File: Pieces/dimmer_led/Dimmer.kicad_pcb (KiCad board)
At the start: 2 copper layers, 83 x 60 mm, 41 parts, among them J1 Conn_01x02_Female, J2 Conn_01X03, J3 TB_1X2, J4 Conn_01x03_Female, J5 TB_1X2, J6 TB_1X2, Q1 BTA06-600C, Q2 BTA06-600C, Q3 BTA06-600C, Q5 2N7000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

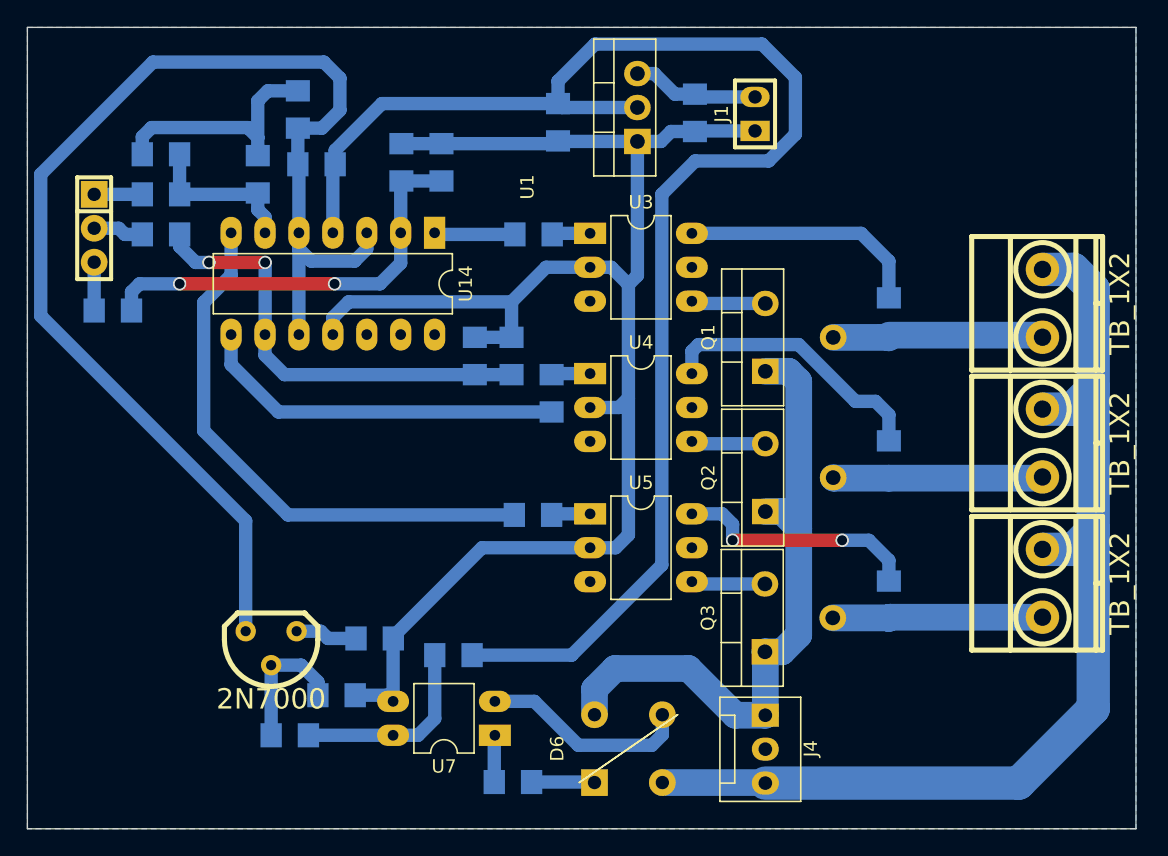
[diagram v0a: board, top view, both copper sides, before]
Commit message: pcb actualizado
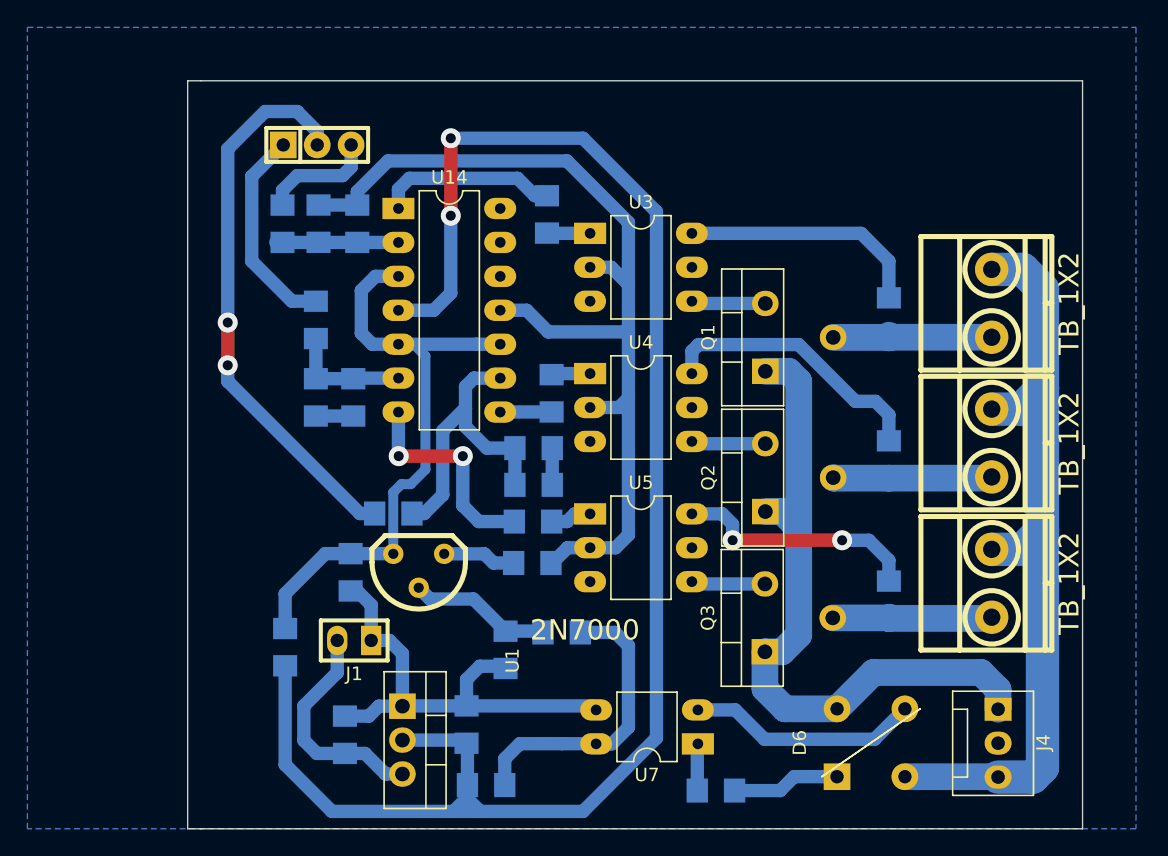
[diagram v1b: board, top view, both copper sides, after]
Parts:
- moved C1 53.4 mm to (131.8, 127.0), turned to -90 degrees
- moved J1 49.5 mm to (132.5, 119.9), turned to 180 degrees
- moved U1 45.8 mm to (136.1, 124.8), turned to -90 degrees
- moved C2 45.6 mm to (140.9, 126.2), turned to -90 degrees
- moved R32 36.2 mm to (127.3, 120.4), turned to -90 degrees
- moved C20 34.9 mm to (132.2, 114.8), turned to 90 degrees
- moved R38 27.2 mm to (135.4, 110.4)
- moved R30 21.8 mm to (148.0, 119.3)
- moved R37 21.6 mm to (129.6, 101.7), turned to 90 degrees
- moved C22 18.2 mm to (132.4, 101.7), turned to 90 degrees
- moved D6 18.2 mm to (171.2, 127.6)
- moved J2 17.8 mm to (129.7, 82.8), turned to 0 degrees
- moved J4 17.4 mm to (180.7, 125.0)
- moved R28 15.2 mm to (159.6, 131.1)
- moved U7 15.2 mm to (158.2, 127.6)
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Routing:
- net /OUT: track 95.6 -> 47.7 mm
- net /Int2: track 3.80 -> 42.0 mm, vias 0 -> 2
- net /OUT_3: track 41.5 -> 16.2 mm, vias 0 -> 2
- net /OUT_2: track 27.7 -> 3.85 mm
- net Net-(C21-Pad1): track 31.6 -> 8.69 mm, vias 2 -> 0
- net GND: track 137.3 -> 115.5 mm
- net Earth: track 79.3 -> 59.7 mm
- net +5V: track 113.0 -> 125.2 mm, vias 0 -> 2
- net /Int3: track 3.61 -> 15.7 mm
- net Net-(C23-Pad1): track 33.8 -> 23.1 mm, vias 2 -> 0
- net +12V: track 9.53 -> 17.2 mm
- net Net-(R29-Pad2): track 14.7 -> 22.3 mm
- net /OUT_1: track 6.06 -> 13.5 mm
- net /Int1: track 3.62 -> 8.63 mm
- net Net-(J5-Pad1): track 15.7 -> 11.9 mm
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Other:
- board size 83 x 60 mm -> 67 x 56 mm
